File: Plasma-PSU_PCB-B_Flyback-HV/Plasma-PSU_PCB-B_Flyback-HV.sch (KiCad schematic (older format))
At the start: 30 parts, among them J101 PWM_IN, J102 PWR_IN, J103 ENBL_IN, Q101 BT169B, Q102 TIP41C, Q103 TIP42C, Q104 BT169B, Q105 IPW60, U101 L7812, U102 L7805, U103 ILD74

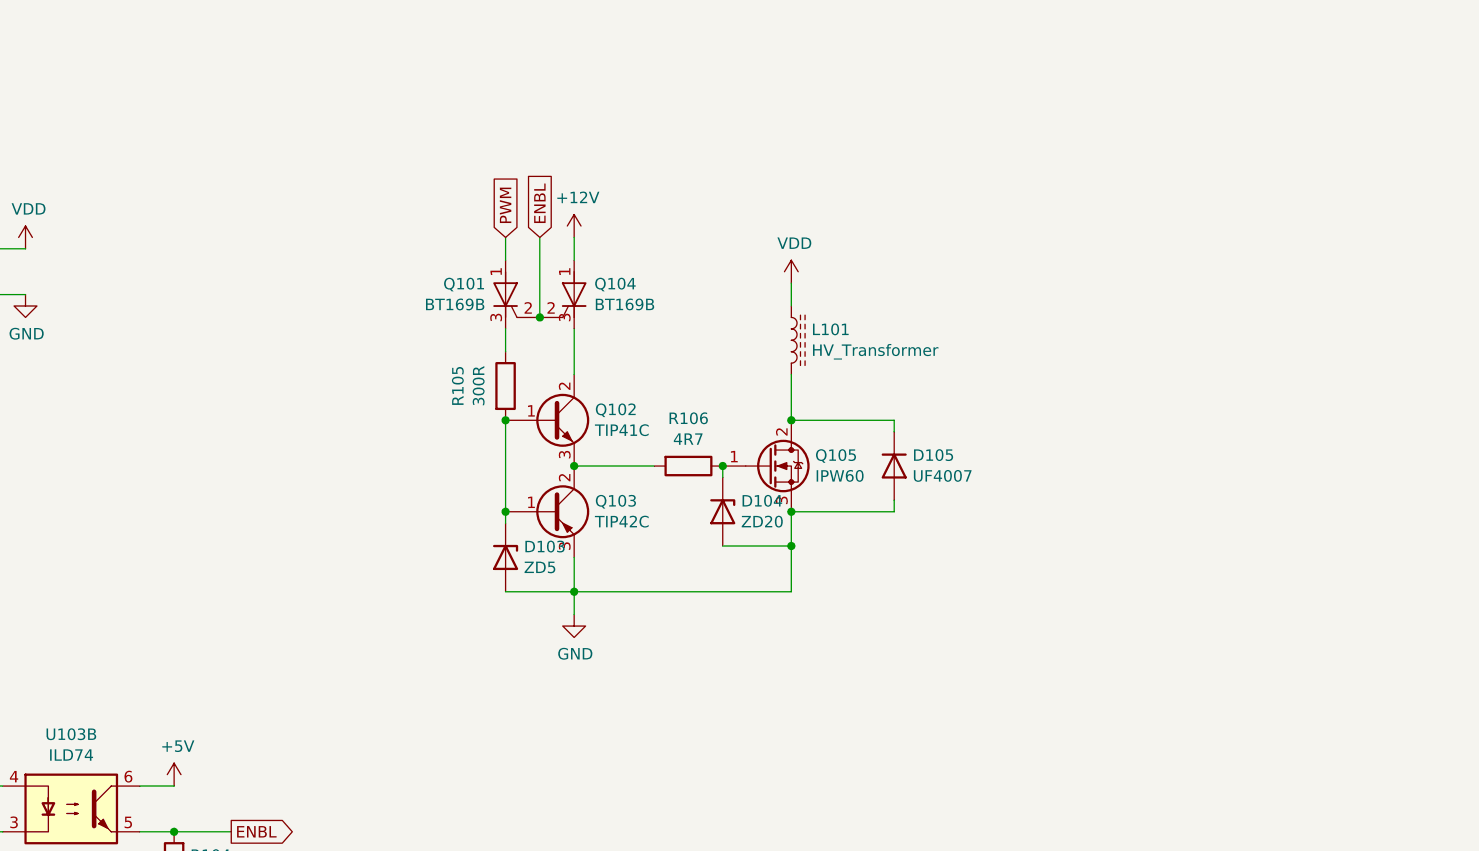
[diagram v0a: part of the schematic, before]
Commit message: Flyback PCB w/ SMD & Earth
- Changed most resistors to SMD
- Included Earth planes separate from GND for shielding
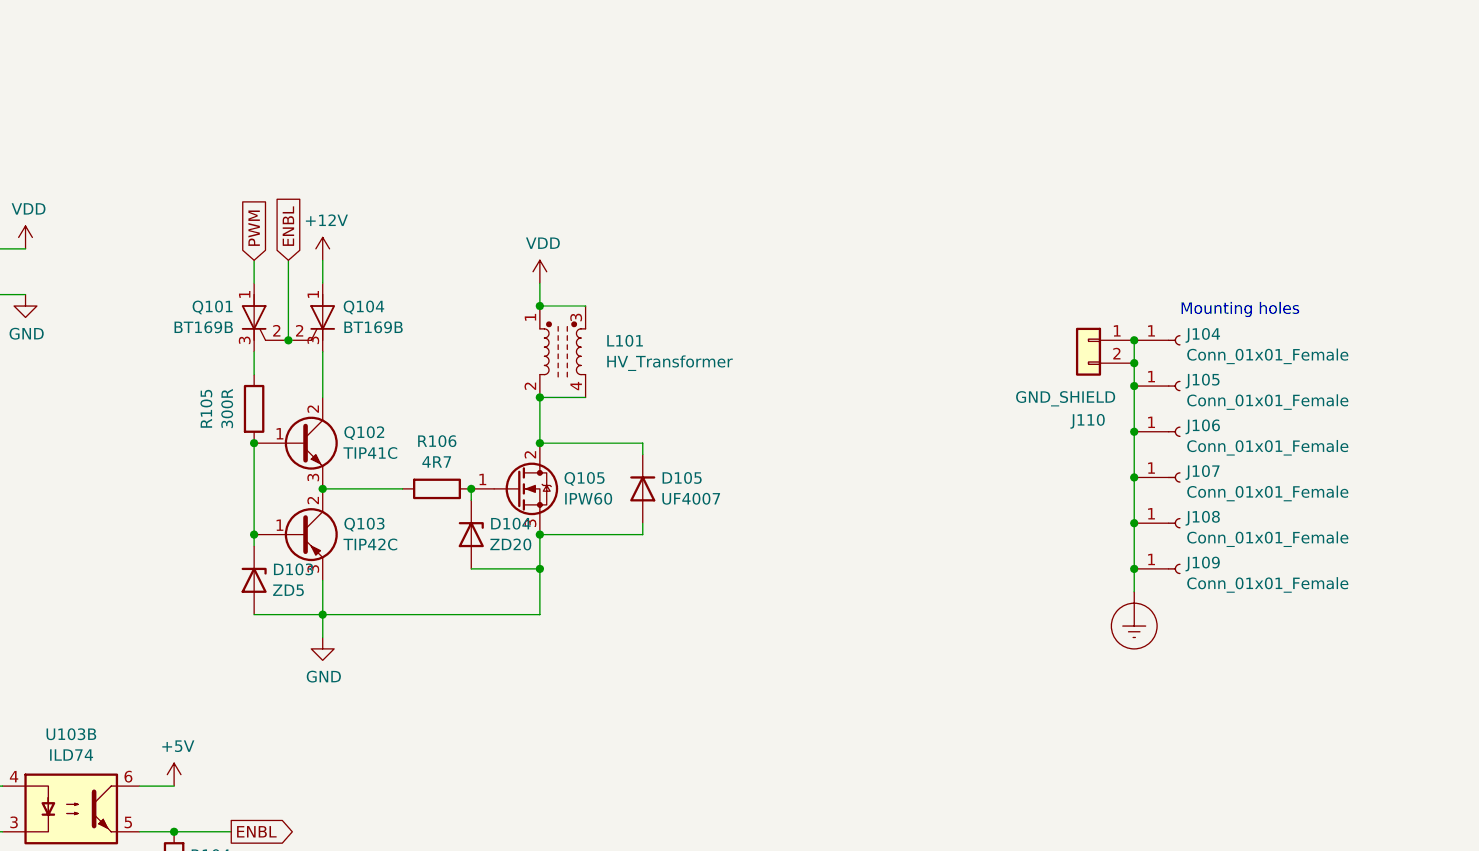
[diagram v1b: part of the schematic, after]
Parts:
- removed L101: HV_Transformer, Plasma-PSU_PCB-B_Flyback-HV:HF-HV_Transformer_15kV_300W, symbol Device:L_Core_Ferrite
- added J104, J105, J106, J107, J108, J109: Conn_01x01_Female, MountingHole:MountingHole_3.2mm_M3_Pad_Via, symbol Connector:Conn_01x01_Female
- added J110: GND_SHIELD, TerminalBlock_Phoenix:TerminalBlock_Phoenix_MKDS-3-2-5.08_1x02_P5.08mm_Horizontal, symbol Connector_Generic:Conn_01x02
- added L101: HV_Transformer, Plasma-PSU_PCB-B_Flyback-HV:HF-HV_Transformer_15kV_300W, symbol Device:L_Core_Ferrite_Coupled
- R101, R102, R103, R104, R105: footprint Resistor_THT:R_Axial_DIN0207_L6.3mm_D2.5mm_P7.62mm_Horizontal -> Resistor_SMD:R_0603_1608Metric
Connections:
- net VDD: now also L101.1, L101.3
- net at D105.1 (K), Q105.2 (D): now also L101.2, L101.4
- new net Earth_Protective: J104.1 (Pin_1), J105.1 (Pin_1), J106.1 (Pin_1), J107.1 (Pin_1), J108.1 (Pin_1), J109.1 (Pin_1), J110.1 (Pin_1), J110.2 (Pin_2)
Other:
- note added: "Mounting holes"
- moved on the sheet: D103, D104, D105, Q101, Q102, Q103, Q104, Q105, R105, R106
